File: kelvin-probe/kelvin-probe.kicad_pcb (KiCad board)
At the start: 2 copper layers, 60 x 21 mm, 4 parts, among them J1 Conn_Coaxial, J2 Conn_Coaxial, J3 Conn_Coaxial, J4 Conn_Coaxial

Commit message: Added more projects.
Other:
- net class Default removed

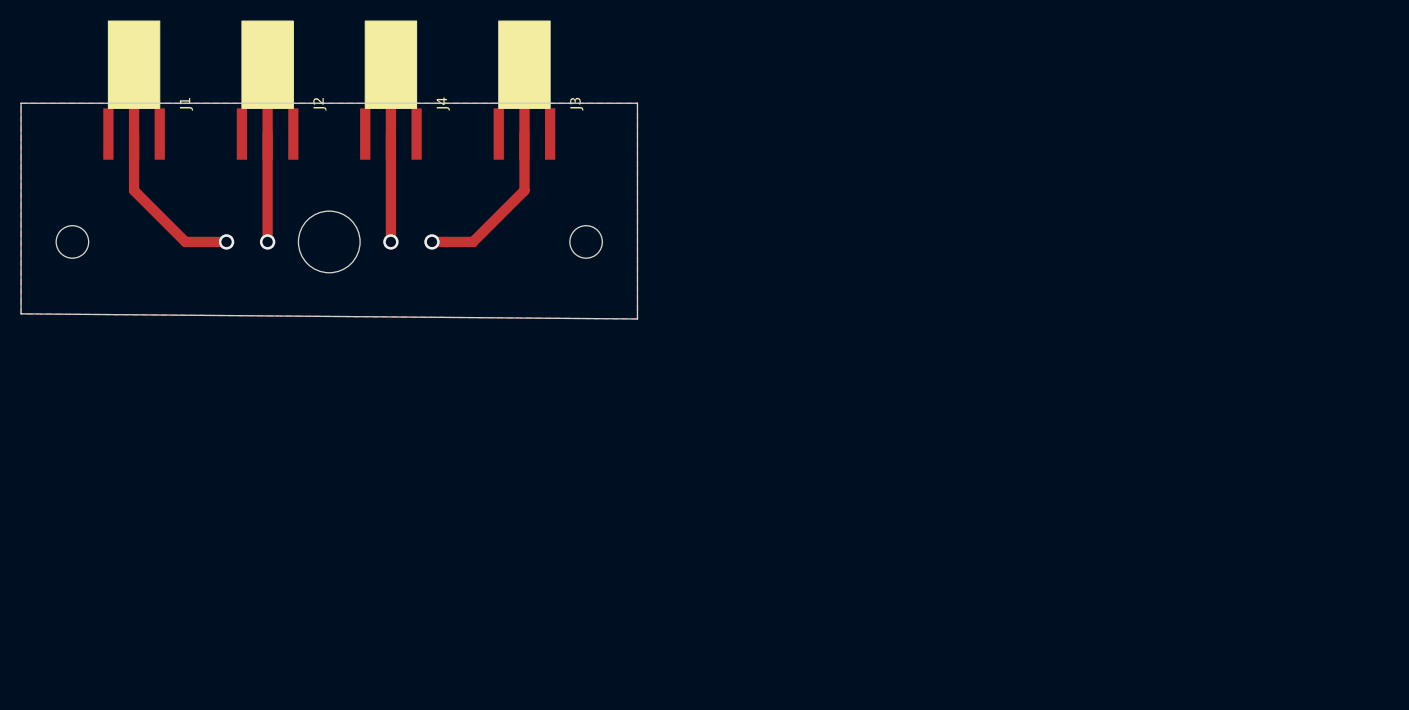
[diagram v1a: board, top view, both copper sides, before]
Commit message: PCB layout refactoring.
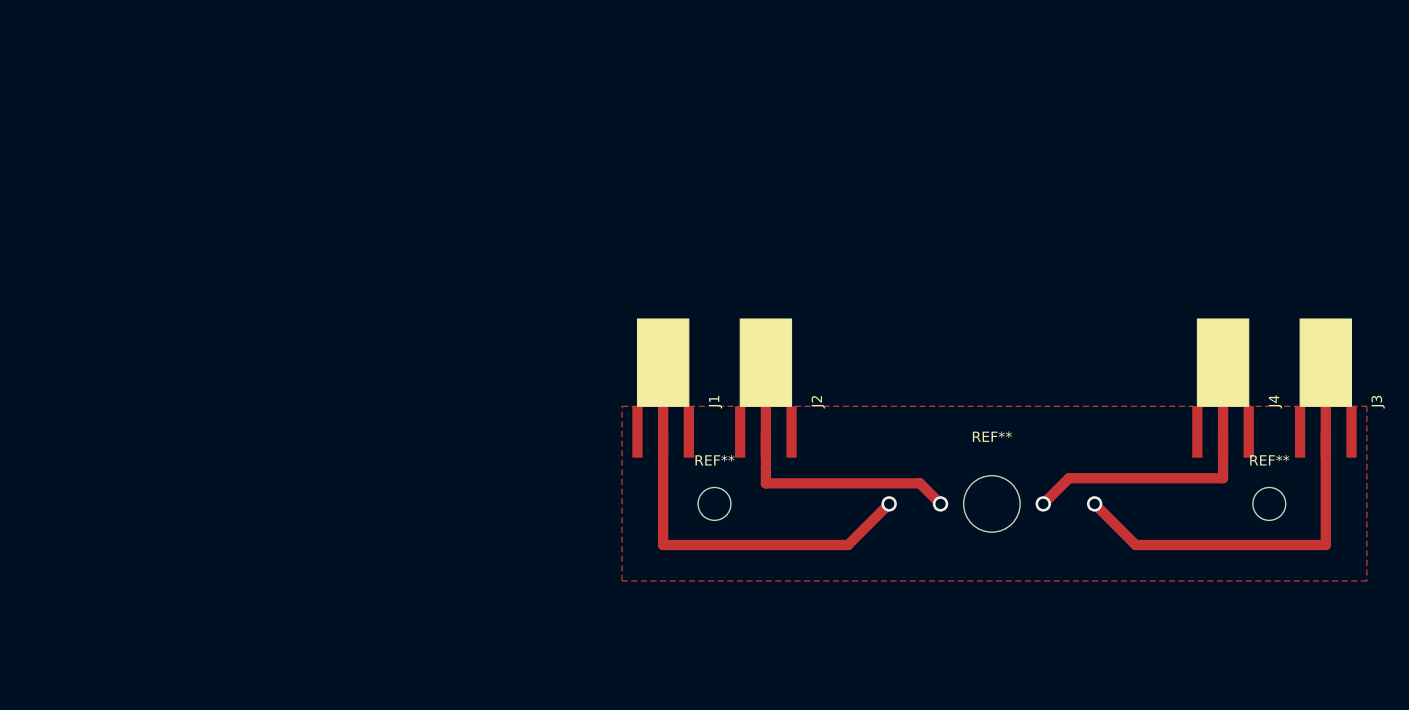
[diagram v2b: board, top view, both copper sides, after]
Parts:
- added REF**: MountingHole_5.5mm, MountingHole:MountingHole_5.5mm, F.Cu at (142.0, 85.0)
- added REF**: MountingHole_3.2mm_M3, MountingHole:MountingHole_3.2mm_M3, F.Cu at (169.0, 85.0)
- added REF**: MountingHole_3.2mm_M3, MountingHole:MountingHole_3.2mm_M3, F.Cu at (115.0, 85.0)
- moved J4 86.0 mm to (170.0, 75.0)
- moved J3 83.2 mm to (180.0, 75.0)
- moved J1 59.1 mm to (115.5, 75.0)
- moved J2 56.5 mm to (125.5, 75.0)
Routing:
- net Net-(IP2-Pad1): track 16.6 -> 35.2 mm
- net Net-(IP1-Pad1): track 16.6 -> 34.7 mm
- net Net-(J4-Pad1): track 10.5 -> 23.0 mm
- net Net-(J2-Pad1): track 10.5 -> 22.8 mm
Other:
- board outline removed
- net class Default added: clearance 0.75, trace_width 1, via_dia 0.8, via_drill 0.4

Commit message: Probe updates. Also suppressed gbr and drl files in git.
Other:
- board outline added: 72.5 x 17 mm
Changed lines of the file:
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@@
   (general
     (thickness 1.6)
-    (drawings 0)
+    (drawings 4)
     (tracks 17)
     (zones 0)
@@
       (net 1 GND))
   )
+  (gr_line (start 106 92.5) (end 106 75.5) (layer Edge.Cuts) (width 0.05))
+  (gr_line (start 178.5 92.5) (end 106 92.5) (layer Edge.Cuts) (width 0.05))
+  (gr_line (start 178.5 75.5) (end 178.5 92.5) (layer Edge.Cuts) (width 0.05))
+  (gr_line (start 106 75.5) (end 178.5 75.5) (layer Edge.Cuts) (width 0.05))
   (via (at 132 85) (size 1.5) (drill 1) (layers F.Cu B.Cu) (net 2))
   (segment (start 132 85) (end 128 89) (width 1) (layer F.Cu) (net 2))

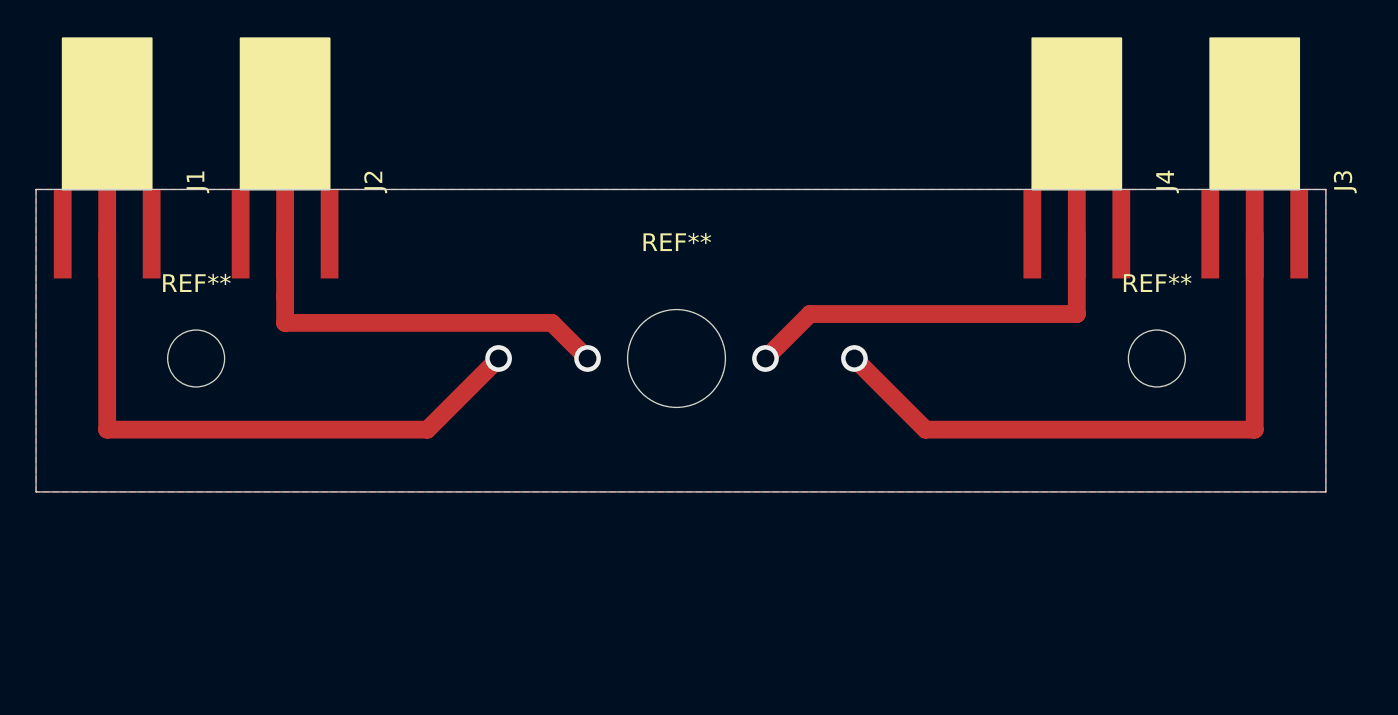
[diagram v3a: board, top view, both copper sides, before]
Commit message: Updated the probe layout.
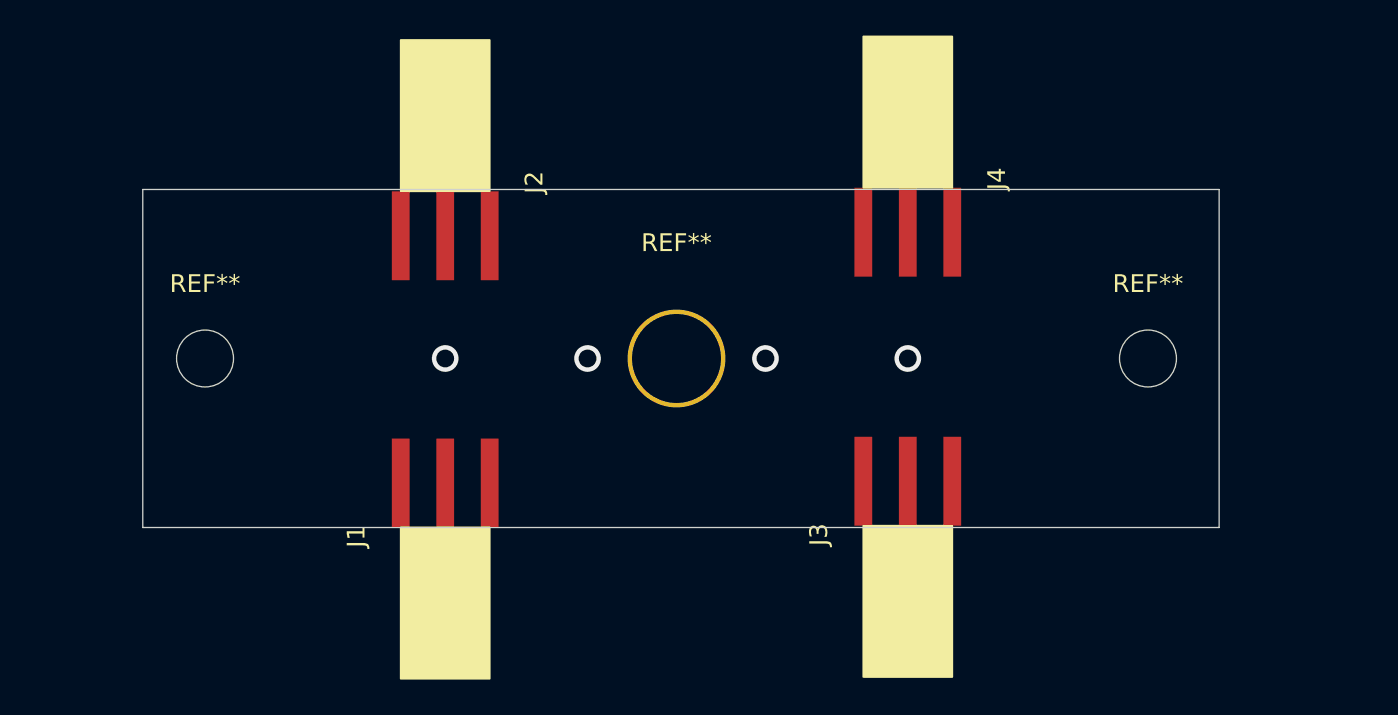
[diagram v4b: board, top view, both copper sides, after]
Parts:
- moved J3 36.4 mm to (149.5, 94.9), turned to 90 degrees
- moved J1 21.5 mm to (123.5, 95.0), turned to 90 degrees
- moved J4 9.50 mm to (160.5, 74.9)
- moved J2 9.00 mm to (134.5, 75.1)
- moved REF** 0.50 mm to (168.5, 85.0)
- moved REF** 0.50 mm to (115.5, 85.0)
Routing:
- net Net-(IP2-Pad1): track 35.2 -> 0.00 mm
- net Net-(IP1-Pad1): track 34.7 -> 0.00 mm
- net Net-(J4-Pad1): track 23.0 -> 0.00 mm
- net Net-(J2-Pad1): track 22.8 -> 0.00 mm
- removed copper zone on F.Cu, net GND
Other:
- board size 72.5 x 17 mm -> 60.5 x 19 mm

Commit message: Local mods.
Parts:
- moved J4 14.0 mm to (174.5, 75.0)
- moved J3 14.0 mm to (163.5, 94.9)
- moved J2 13.5 mm to (121.0, 75.0)
- moved J1 13.5 mm to (110.0, 95.0)
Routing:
- net Net-(J4-Pad1): track 0.00 -> 24.5 mm
- net Net-(J2-Pad1): track 0.00 -> 24.0 mm
- net Net-(IP2-Pad1): track 0.00 -> 17.7 mm
- net Net-(IP1-Pad1): track 0.00 -> 17.3 mm
- added copper zone on F.Cu, net GND
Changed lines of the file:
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@@
     (thickness 1.6)
     (drawings 4)
-    (tracks 4)
+    (tracks 21)
     (zones 0)
     (modules 7)
@@
   )
   (module custom-footprints:amazon-sma-connector (layer F.Cu)
-    (at 134.5 75.1 270)
+    (at 121 75 270)
     (fp_text reference J2 (at 0 0.5 90) (layer F.SilkS)
       (effects (font (size 1 1) (thickness 0.15)))
@@
       (effects (font (size 1 1) (thickness 0.15)))
     )
+    (fp_circle (center 0 0) (end 3.45 0) (layer F.CrtYd) (width 0.05))
     (fp_circle (center 0 0) (end 3.2 0) (layer Cmts.User) (width 0.15))
-    (fp_circle (center 0 0) (end 3.45 0) (layer F.CrtYd) (width 0.05))
     (fp_text user %R (at 0.3 0) (layer F.Fab)
       (effects (font (size 1 1) (thickness 0.15)))
@@
       (effects (font (size 1 1) (thickness 0.15)))
     )
+    (fp_circle (center 0 0) (end 3.2 0) (layer Cmts.User) (width 0.15))
+    (fp_circle (center 0 0) (end 3.45 0) (layer F.CrtYd) (width 0.05))
     (fp_text user %R (at 0.3 0) (layer F.Fab)
       (effects (font (size 1 1) (thickness 0.15)))
     )
-    (fp_circle (center 0 0) (end 3.45 0) (layer F.CrtYd) (width 0.05))
-    (fp_circle (center 0 0) (end 3.2 0) (layer Cmts.User) (width 0.15))
     (pad "" np_thru_hole circle (at 0 0) (size 3.2 3.2) (drill 3.2) (layers *.Cu *.Mask))
   )
@@
       (effects (font (size 1 1) (thickness 0.15)))
     )
+    (fp_circle (center 0 0) (end 5.75 0) (layer F.CrtYd) (width 0.05))
     (fp_circle (center 0 0) (end 5.5 0) (layer Cmts.User) (width 0.15))
-    (fp_circle (center 0 0) (end 5.75 0) (layer F.CrtYd) (width 0.05))
     (fp_text user %R (at 0.3 0) (layer F.Fab)
       (effects (font (size 1 1) (thickness 0.15)))
@@
   )
   (module custom-footprints:amazon-sma-connector (layer F.Cu)
-    (at 160.5 74.9 270)
+    (at 174.5 75 270)
     (fp_text reference J4 (at 0 0.5 90) (layer F.SilkS)
       (effects (font (size 1 1) (thickness 0.15)))
@@
   )
   (module custom-footprints:amazon-sma-connector (layer F.Cu)
-    (at 149.5 94.9 90)
+    (at 163.5 94.9 90)
     (fp_text reference J3 (at 0 0.5 90) (layer F.SilkS)
       (effects (font (size 1 1) (thickness 0.15)))
@@
   )
   (module custom-footprints:amazon-sma-connector (layer F.Cu)
-    (at 123.5 95 90)
+    (at 110 95 90)
     (fp_text reference J1 (at 0 0.5 90) (layer F.SilkS)
       (effects (font (size 1 1) (thickness 0.15)))
@@
   (gr_line (start 172.5 94.5) (end 112 94.5) (layer Edge.Cuts) (width 0.05))
   (gr_line (start 172.5 75.5) (end 172.5 94.5) (layer Edge.Cuts) (width 0.05))
-  (via (at 129 85) (size 1.5) (drill 1) (layers F.Cu B.Cu) (net 2))
-  (via (at 137 85) (size 1.5) (drill 1) (layers F.Cu B.Cu) (net 3))
-  (via (at 155 85) (size 1.5) (drill 1) (layers F.Cu B.Cu) (net 4))
-  (via (at 147 85) (size 1.5) (drill 1) (layers F.Cu B.Cu) (net 5))
+  (via (at 128.25 85) (size 2.5) (drill 1.5) (layers F.Cu B.Cu) (net 2))
+  (segment (start 115.5 89.249998) (end 115.5 92) (width 1) (layer F.Cu) (net 2))
+  (segment (start 119.749998 85) (end 115.5 89.249998) (width 1) (layer F.Cu) (net 2))
+  (segment (start 128.25 85) (end 119.749998 85) (width 1) (layer F.Cu) (net 2))
+  (via (at 135 85) (size 2.5) (drill 1.5) (layers F.Cu B.Cu) (net 3))
+  (segment (start 115.5 80.750002) (end 115.5 78) (width 1) (layer F.Cu) (net 3))
+  (segment (start 132.149999 82.149999) (end 116.899997 82.149999) (width 1) (layer F.Cu) (net 3))
+  (segment (start 116.899997 82.149999) (end 115.5 80.750002) (width 1) (layer F.Cu) (net 3))
+  (segment (start 135 85) (end 132.149999 82.149999) (width 1) (layer F.Cu) (net 3))
+  (via (at 155.75 85) (size 2.5) (drill 1.5) (layers F.Cu B.Cu) (net 4))
+  (segment (start 169 89.149998) (end 169 91.9) (width 1) (layer F.Cu) (net 4))
+  (segment (start 168.000001 88.149999) (end 169 89.149998) (width 1) (layer F.Cu) (net 4))
+  (segment (start 158.899999 88.149999) (end 168.000001 88.149999) (width 1) (layer F.Cu) (net 4))
+  (segment (start 155.75 85) (end 158.899999 88.149999) (width 1) (layer F.Cu) (net 4))
+  (via (at 149 85) (size 2.5) (drill 1.5) (layers F.Cu B.Cu) (net 5))
+  (segment (start 169 80.750002) (end 169 78) (width 1) (layer F.Cu) (net 5))
+  (segment (start 168.000001 81.750001) (end 169 80.750002) (width 1) (layer F.Cu) (net 5))
+  (segment (start 165.999999 81.750001) (end 168.000001 81.750001) (width 1) (layer F.Cu) (net 5))
+  (segment (start 165.250001 82.499999) (end 165.999999 81.750001) (width 1) (layer F.Cu) (net 5))
+  (segment (start 151.500001 82.499999) (end 165.250001 82.499999) (width 1) (layer F.Cu) (net 5))
+  (segment (start 149 85) (end 151.500001 82.499999) (width 1) (layer F.Cu) (net 5))
+  (zone (net 1) (net_name GND) (layer F.Cu) (hatch edge 0.508)
+    (connect_pads (clearance 0.508))
+    (min_thickness 0.254)
+    (fill yes (arc_segments 32) (thermal_gap 0.508) (thermal_bridge_width 0.508))
+    (polygon
+      (pts
+        (xy 172.5 94.5) (xy 112 94.5) (xy 112 75.5) (xy 172.5 75.5)
+      )
+    )
+  )
 )
